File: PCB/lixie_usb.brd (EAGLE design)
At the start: 20.3 x 38 mm, 5 parts, among them U2 AT90USB162-16AU

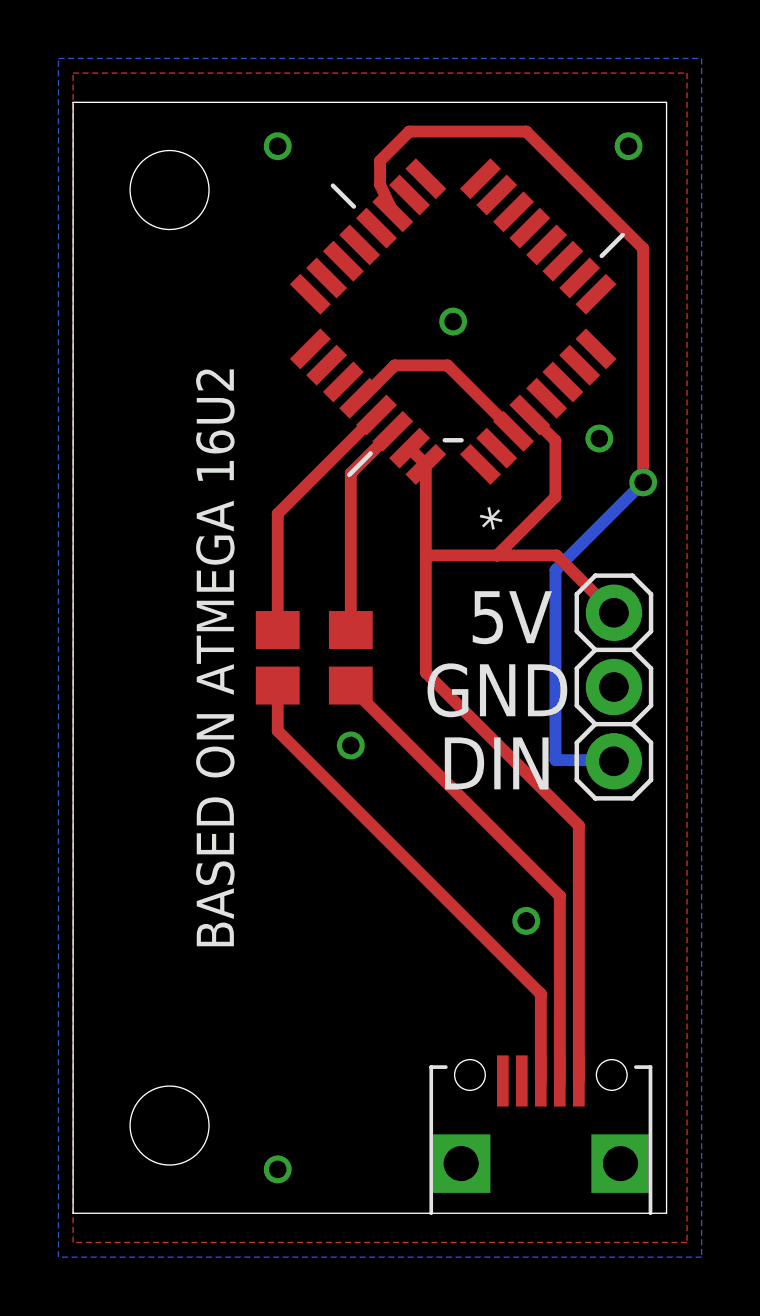
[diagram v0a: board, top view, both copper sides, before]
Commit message: Switched pin order to standard
Power/ground/data order changed to power/data/ground.
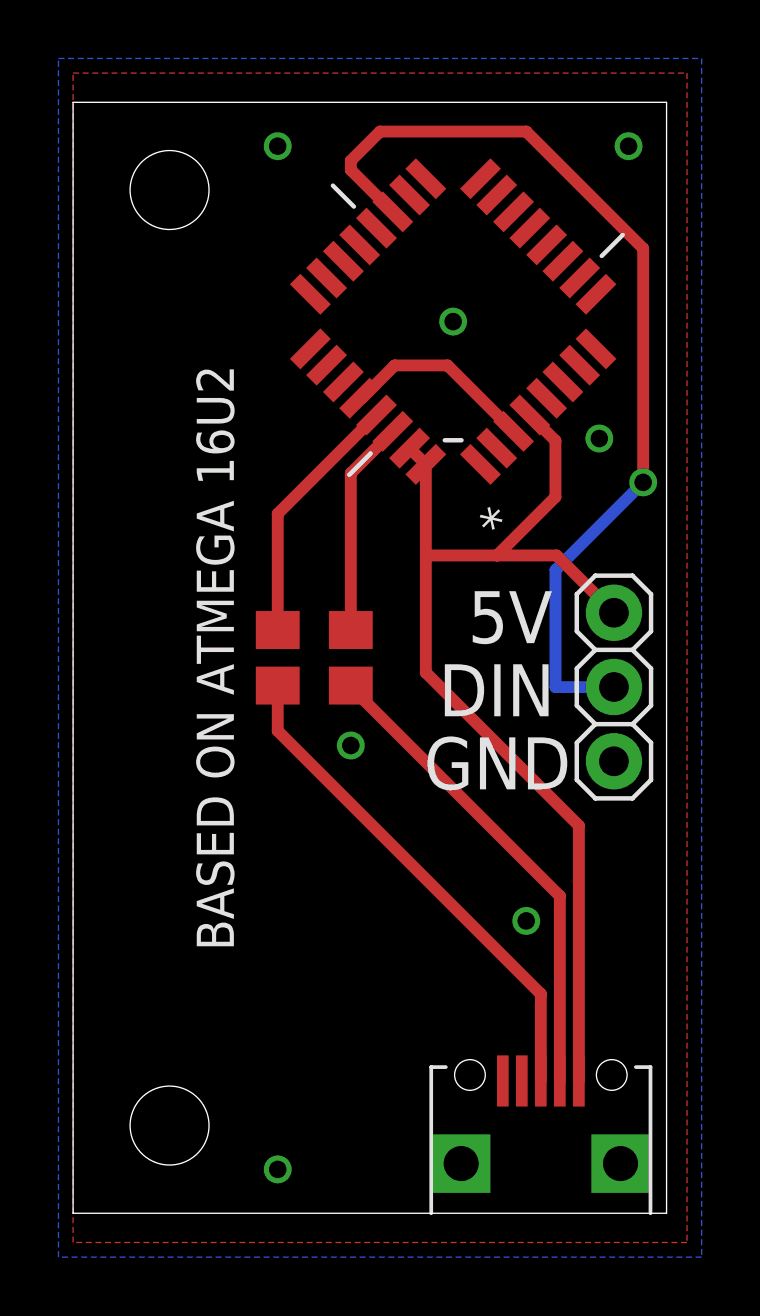
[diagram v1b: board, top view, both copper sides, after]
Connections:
- net N$20 renamed 5V
- removed net N$23: JP1.1, U2.19
- new net DOUT: JP1.2, U2.19
- net GND: now also JP1.1; no longer JP1.2
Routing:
- net N$23: track 33.7 -> 0.00 mm, vias 1 -> 0
- net DOUT: track 0.00 -> 32.7 mm, vias 0 -> 1
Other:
- board text added: "Last Updated: December 18th, 2016"
- board text removed: "Last Updated: December 11th, 2016"
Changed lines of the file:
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@@
 <?xml version="1.0" encoding="utf-8"?>
 <!DOCTYPE eagle SYSTEM "eagle.dtd">
-<eagle version="7.6.0">
+<eagle version="7.7.0">
 <drawing>
 <settings>
@@
 <text x="21.5" y="0" size="1.27" layer="51" font="vector">Released under the GPLv3 License</text>
 <text x="21.5" y="3" size="1.27" layer="51" font="vector" ratio="11">Last Updated:
-December 11th, 2016</text>
+December 18th, 2016</text>
 <text x="13.5" y="19.5" size="1.778" layer="25" font="vector">5V</text>
-<text x="12" y="17" size="1.778" layer="25" font="vector">GND</text>
-<text x="12.5" y="14.5" size="1.778" layer="25" font="vector">DIN</text>
+<text x="12" y="14.5" size="1.778" layer="25" font="vector">GND</text>
+<text x="12.5" y="17" size="1.778" layer="25" font="vector">DIN</text>
 <text x="3.5" y="19" size="2.54" layer="29" font="vector" ratio="10" rot="R90" align="bottom-center">LIXIE USB</text>
 <text x="5.5" y="19" size="1.27" layer="25" font="vector" rot="R90" align="bottom-center">BASED ON ATMEGA 16U2</text>
@@
 </elements>
 <signals>
-<signal name="N$20">
+<signal name="5V">
 <contactref element="JP1" pad="3"/>
 <contactref element="JP2" pad="5"/>
@@
 </signal>
 <signal name="GND">
-<contactref element="JP1" pad="2"/>
 <polygon width="0.254" layer="1">
 <vertex x="21" y="-1"/>
@@
 <via x="15.5" y="10" extent="1-16" drill="0.6"/>
 <via x="18" y="26.5" extent="1-16" drill="0.6"/>
-</signal>
-<signal name="N$23">
 <contactref element="JP1" pad="1"/>
-<contactref element="U2" pad="19"/>
-<wire x1="10.934540625" y1="34.253746875" x2="10.5" y2="35.1882875" width="0.4064" layer="1"/>
-<wire x1="10.5" y1="35.1882875" x2="10.5" y2="36" width="0.4064" layer="1"/>
-<wire x1="10.5" y1="36" x2="11.5" y2="37" width="0.4064" layer="1"/>
-<wire x1="11.5" y1="37" x2="15.5" y2="37" width="0.4064" layer="1"/>
-<wire x1="15.5" y1="37" x2="19.5" y2="33" width="0.4064" layer="1"/>
-<wire x1="19.5" y1="33" x2="19.5" y2="25" width="0.4064" layer="1"/>
-<via x="19.5" y="25" extent="1-16" drill="0.6"/>
-<wire x1="19.5" y1="25" x2="16.5" y2="22" width="0.4064" layer="16"/>
-<wire x1="16.5" y1="22" x2="16.5" y2="15.5" width="0.4064" layer="16"/>
-<wire x1="16.5" y1="15.5" x2="18.5" y2="15.5" width="0.4064" layer="16"/>
-<wire x1="18.5" y1="15.5" x2="18.5" y2="15.46" width="0.4064" layer="16"/>
 </signal>
 <signal name="N$7">
@@
 <wire x1="7" y1="16.5" x2="7" y2="18.05" width="0.4064" layer="1"/>
 </signal>
+<signal name="DOUT">
+<contactref element="U2" pad="19"/>
+<contactref element="JP1" pad="2"/>
+<wire x1="18.5" y1="18" x2="16.5" y2="18" width="0.4064" layer="16"/>
+<wire x1="16.5" y1="18" x2="16.5" y2="22" width="0.4064" layer="16"/>
+<wire x1="19.5" y1="33" x2="15.5" y2="37" width="0.4064" layer="1"/>
+<wire x1="15.5" y1="37" x2="10.5" y2="37" width="0.4064" layer="1"/>
+<wire x1="10.5" y1="37" x2="9.5" y2="36" width="0.4064" layer="1"/>
+<wire x1="9.5" y1="36" x2="9.5" y2="35.6882875" width="0.4064" layer="1"/>
+<wire x1="9.5" y1="35.6882875" x2="10.934540625" y2="34.253746875" width="0.4064" layer="1"/>
+<wire x1="19.5" y1="33" x2="19.5" y2="25" width="0.4064" layer="1"/>
+<via x="19.5" y="25" extent="1-16" drill="0.6"/>
+<wire x1="19.5" y1="25" x2="16.5" y2="22" width="0.4064" layer="16"/>
+</signal>
 </signals>
